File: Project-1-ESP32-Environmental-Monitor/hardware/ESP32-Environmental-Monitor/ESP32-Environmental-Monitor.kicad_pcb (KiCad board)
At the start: 2 copper layers, 5 parts, among them U1 AM2302, U2 ESP32-WROOM-32

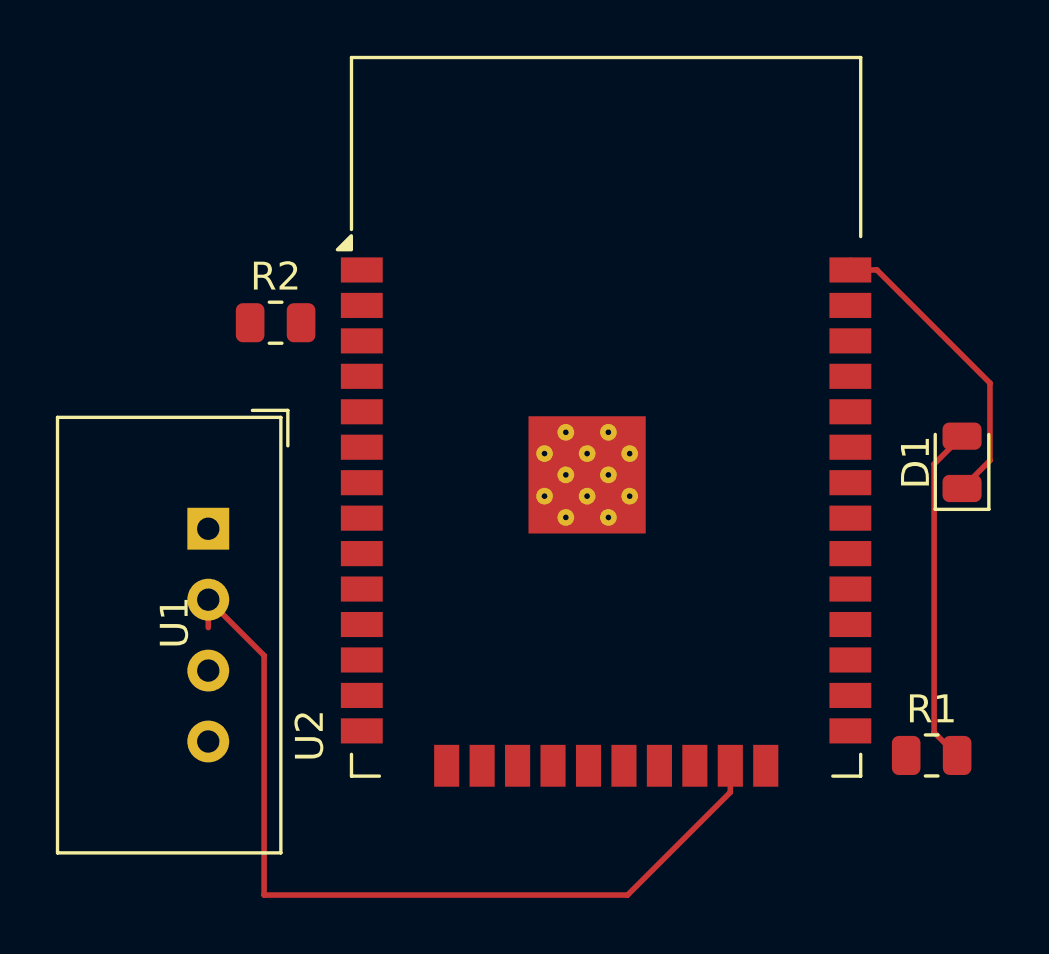
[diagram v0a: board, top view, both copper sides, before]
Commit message: Complete PCB routing - all connections done
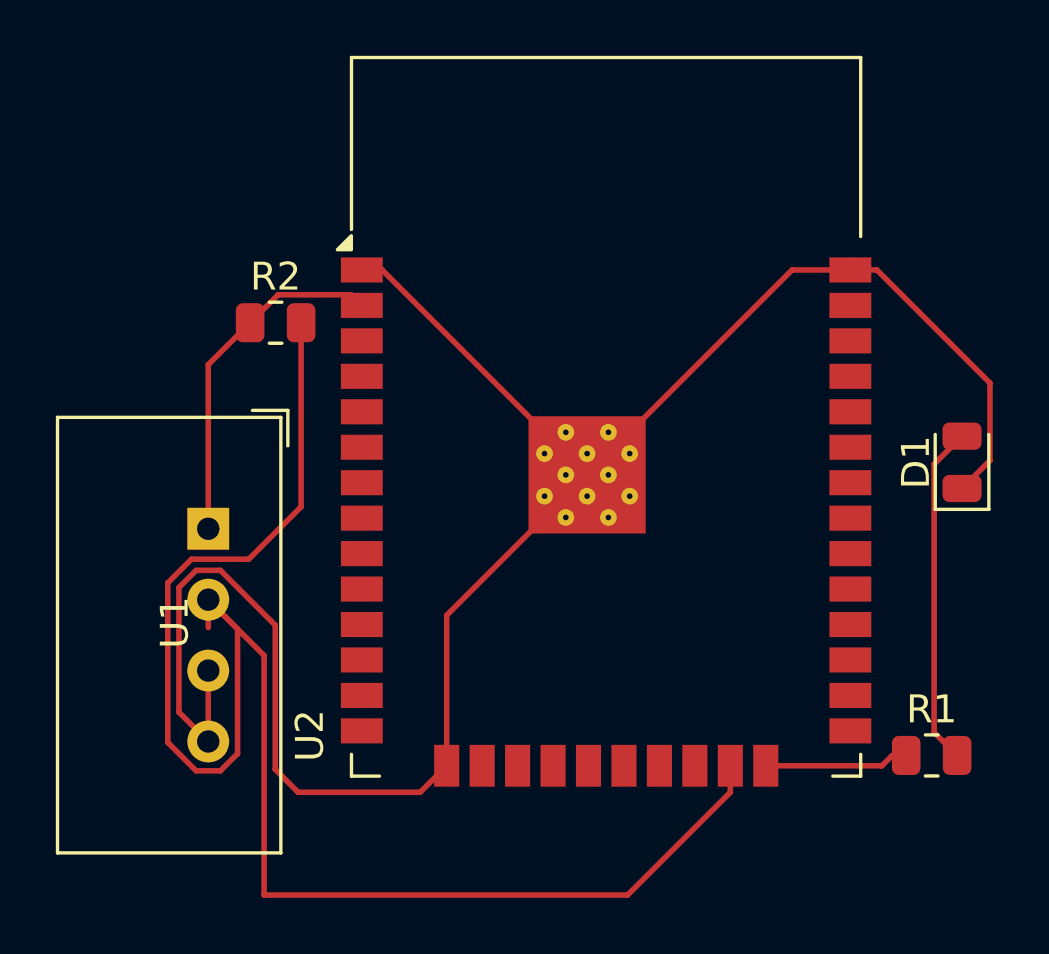
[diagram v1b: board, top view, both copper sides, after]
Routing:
- net GND: track 11.2 -> 65.9 mm
- net Net-(U1-SDA): track 31.6 -> 58.9 mm
- net VCC: track 0.00 -> 12.6 mm
- net Net-(U2-IO2): track 0.00 -> 5.18 mm
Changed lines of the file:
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@@
+	)
+	(segment
+		(start 127.23 92.61)
+		(end 126.5 92.61)
+		(width 0.2)
+		(layer "F.Cu")
+		(net "GND")
 	)
 	(segment
@@
 	)
 	(segment
+		(start 119.95 103.985075)
+		(end 119.95 108.45)
+		(width 0.2)
+		(layer "F.Cu")
+		(net "GND")
+	)
+	(segment
 		(start 144 92.61)
 		(end 144.95 92.61)
@@
 	)
 	(segment
+		(start 129.54 110.37)
+		(end 128.59 111.32)
+		(width 0.2)
+		(layer "F.Cu")
+		(net "GND")
+	)
+	(segment
+		(start 121.434925 103.37)
+		(end 120.565075 103.37)
+		(width 0.2)
+		(layer "F.Cu")
+		(net "GND")
+	)
+	(segment
+		(start 141.91 92.61)
+		(end 144 92.61)
+		(width 0.2)
+		(layer "F.Cu")
+		(net "GND")
+	)
+	(segment
+		(start 129.54 104.98)
+		(end 133.045 101.475)
+		(width 0.2)
+		(layer "F.Cu")
+		(net "GND")
+	)
+	(segment
+		(start 119.95 108.45)
+		(end 121 109.5)
+		(width 0.2)
+		(layer "F.Cu")
+		(net "GND")
+	)
+	(segment
+		(start 136.095 98.425)
+		(end 141.91 92.61)
+		(width 0.2)
+		(layer "F.Cu")
+		(net "GND")
+	)
+	(segment
 		(start 148 100.4375)
 		(end 149 99.4375)
@@
 	)
 	(segment
+		(start 129.54 110.37)
+		(end 129.54 104.98)
+		(width 0.2)
+		(layer "F.Cu")
+		(net "GND")
+	)
+	(segment
+		(start 128.59 111.32)
+		(end 124.22 111.32)
+		(width 0.2)
+		(layer "F.Cu")
+		(net "GND")
+	)
+	(segment
+		(start 120.565075 103.37)
+		(end 119.95 103.985075)
+		(width 0.2)
+		(layer "F.Cu")
+		(net "GND")
+	)
+	(segment
+		(start 123.4 105.335075)
+		(end 121.434925 103.37)
+		(width 0.2)
+		(layer "F.Cu")
+		(net "GND")
+	)
+	(segment
 		(start 149 99.4375)
 		(end 149 96.66)
@@
 	)
 	(segment
+		(start 121 109.5)
+		(end 121 106.96)
+		(width 0.2)
+		(layer "F.Cu")
+		(net "GND")
+	)
+	(segment
 		(start 149 96.66)
 		(end 144.95 92.61)
@@
 	)
 	(segment
+		(start 123.4 110.5)
+		(end 123.4 105.335075)
+		(width 0.2)
+		(layer "F.Cu")
+		(net "GND")
+	)
+	(segment
+		(start 133.045 98.425)
+		(end 127.23 92.61)
+		(width 0.2)
+		(layer "F.Cu")
+		(net "GND")
+	)
+	(segment
+		(start 124.22 111.32)
+		(end 123.4 110.5)
+		(width 0.2)
+		(layer "F.Cu")
+		(net "GND")
+	)
+	(segment
 		(start 147 109.175)
 		(end 147 99.5625)
@@
 	)
 	(segment
+		(start 145.13 110.37)
+		(end 140.97 110.37)
+		(width 0.2)
+		(layer "F.Cu")
+		(net "Net-(U2-IO2)")
+	)
+	(segment
+		(start 145.5 110)
+		(end 145.13 110.37)
+		(width 0.2)
+		(layer "F.Cu")
+		(net "Net-(U2-IO2)")
+	)
+	(segment
+		(start 146 110)
+		(end 145.5 110)
+		(width 0.2)
+		(layer "F.Cu")
+		(net "Net-(U2-IO2)")
+	)
+	(segment
+		(start 121 101.88)
+		(end 121 96)
+		(width 0.2)
+		(layer "F.Cu")
+		(net "VCC")
+	)
+	(segment
+		(start 126.12 93.5)
+		(end 126.5 93.88)
+		(width 0.2)
+		(layer "F.Cu")
+		(net "VCC")
+	)
+	(segment
+		(start 121 96)
+		(end 122.5 94.5)
+		(width 0.2)
+		(layer "F.Cu")
+		(net "VCC")
+	)
+	(segment
+		(start 123.5 93.5)
+		(end 126.12 93.5)
+		(width 0.2)
+		(layer "F.Cu")
+		(net "VCC")
+	)
+	(segment
+		(start 122.5 94.5)
+		(end 123.5 93.5)
+		(width 0.2)
+		(layer "F.Cu")
+		(net "VCC")
+	)
+	(segment
+		(start 122.45 102.97)
+		(end 124.325 101.095)
+		(width 0.2)
+		(layer "F.Cu")
+		(net "Net-(U1-SDA)")
+	)
+	(segment
 		(start 121 104.42)
 		(end 121 105.42)
@@
 	)
 	(segment
+		(start 120.39939 102.97)
+		(end 122.45 102.97)
+		(width 0.2)
+		(layer "F.Cu")
+		(net "Net-(U1-SDA)")
+	)
+	(segment
 		(start 139.7 111.32)
 		(end 139.7 110.37)
@@
 	)
 	(segment
+		(start 122.05 109.934925)
+		(end 121.434925 110.55)
+		(width 0.2)
+		(layer "F.Cu")
+		(net "Net-(U1-SDA)")
+	)
+	(segment
 		(start 123 106.42)
 		(end 123 115)
@@
 	)
 	(segment
+		(start 120.565075 110.55)
+		(end 119.55 109.534925)
+		(width 0.2)
+		(layer "F.Cu")
+		(net "Net-(U1-SDA)")
+	)
+	(segment
+		(start 121.434925 110.55)
+		(end 120.565075 110.55)
+		(width 0.2)
+		(layer "F.Cu")
+		(net "Net-(U1-SDA)")
+	)
+	(segment
+		(start 119.55 109.534925)
+		(end 119.55 103.819389)
+		(width 0.2)
+		(layer "F.Cu")
+		(net "Net-(U1-SDA)")
+	)
+	(segment
+		(start 119.55 103.819389)
+		(end 120.39939 102.97)
+		(width 0.2)
+		(layer "F.Cu")
+		(net "Net-(U1-SDA)")
+	)
+	(segment
+		(start 121 104.42)
+		(end 122.05 105.47)
+		(width 0.2)
+		(layer "F.Cu")
+		(net "Net-(U1-SDA)")
+	)
+	(segment
+		(start 124.325 101.095)
+		(end 124.325 94.5)
+		(width 0.2)
+		(layer "F.Cu")
+		(net "Net-(U1-SDA)")
+	)
+	(segment
 		(start 121 104.42)
 		(end 123 106.42)
 		(width 0.2)
 		(layer "F.Cu")
+		(net "Net-(U1-SDA)")
+	)
+	(segment
+		(start 122.05 105.47)
+		(end 122.05 109.934925)
+		(width 0.2)
+		(layer "F.Cu")
